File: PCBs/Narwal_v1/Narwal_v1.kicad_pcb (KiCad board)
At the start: 4 copper layers, 85 x 100 mm, 48 parts, among them IC1 SWITCH-HSWA4-63DR+, IC2 SWITCH-HSWA4-63DR+, J1 SMA-LPRS-CONNECTOR, J2 Conn_01x04, J3 Conn_01x04, SW1 SW_SPST, U1 HMC452ST89ETR, U2 PGA-103+, U3 RFM96W-433S2, U4 DS3231M

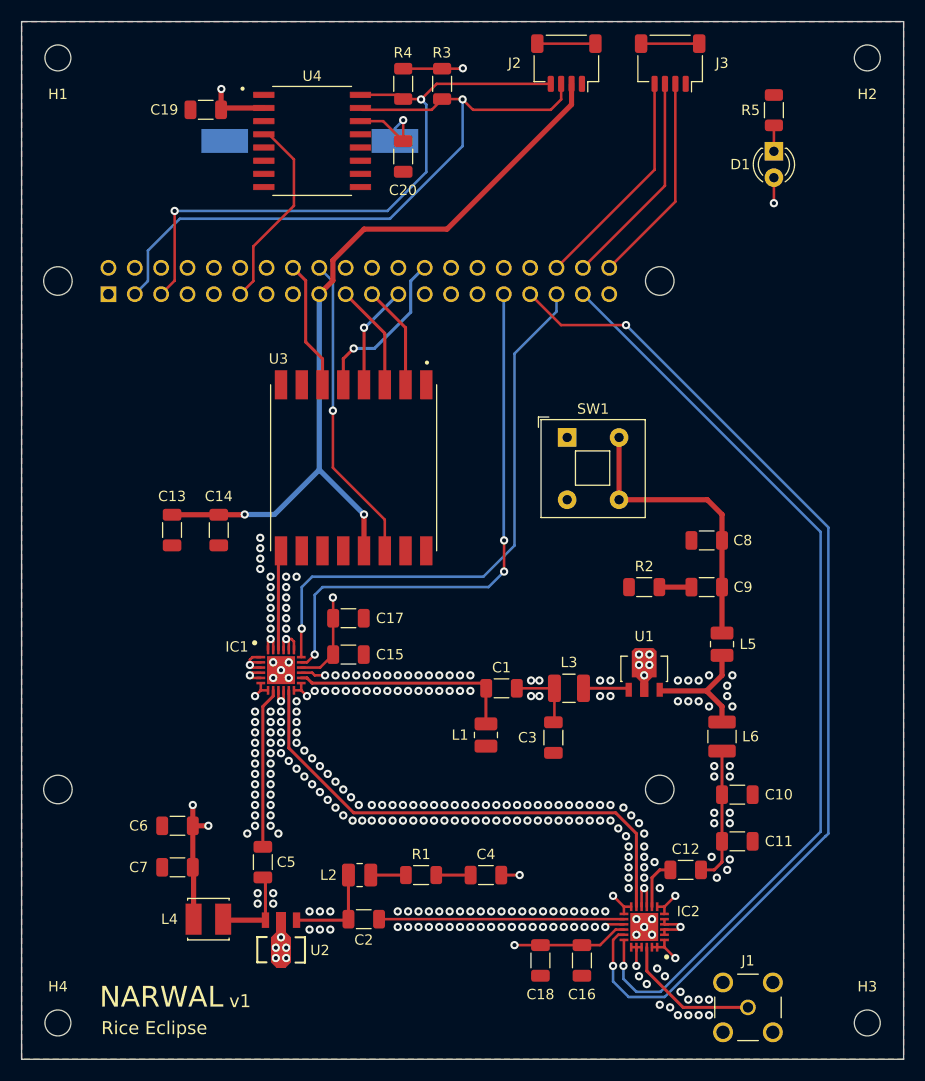
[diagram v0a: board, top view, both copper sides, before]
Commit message: power switch fixes, JLC compatibility changes
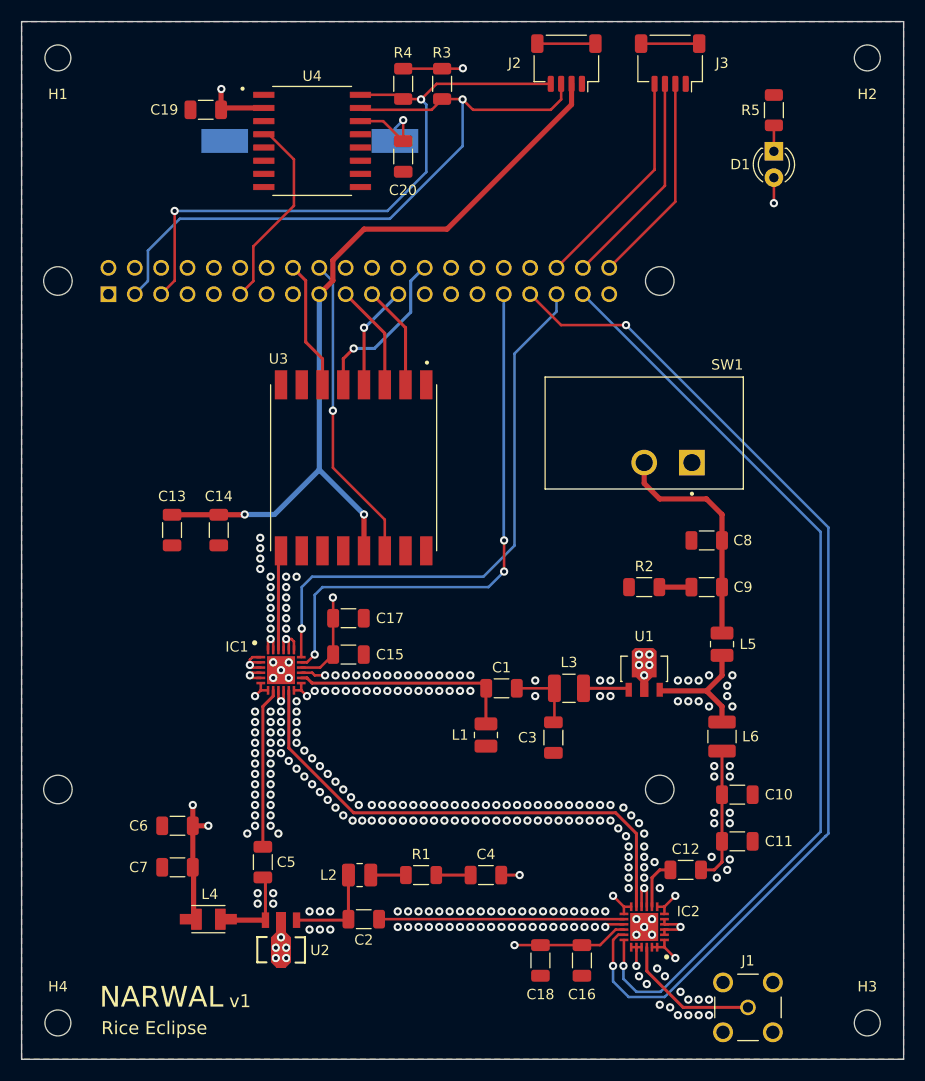
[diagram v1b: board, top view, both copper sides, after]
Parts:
- L4: value CHOKE-LQH44PN4R7MP0L -> CHOKE-LQH32NH4R7J23L; footprint Eclipse_RF_Footprints:CHOKE-LQH44PN4R7MP0L -> Eclipse_RF_Footprints:CHOKE-LQH32NH4R7J23L
- SW1: footprint Button_Switch_THT:SW_Push_2P1T_Toggle_CK_PVA1xxH1xxxxxxV2 -> Eclipse_RF_Footprints:SWITCH-L101011MS02Q
- moved SW1 7.43 mm to (160.0, 89.7), turned to 180 degrees
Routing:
- net Net-(C8-Pad1): track 27.9 -> 22.2 mm
- net GND: vias 299 -> 297
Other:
- rule pad_to_mask_clearance: 0 -> 0.05
- board text added: "JLCJLCJLCJLC"

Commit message: JLC-required silkscreen changes
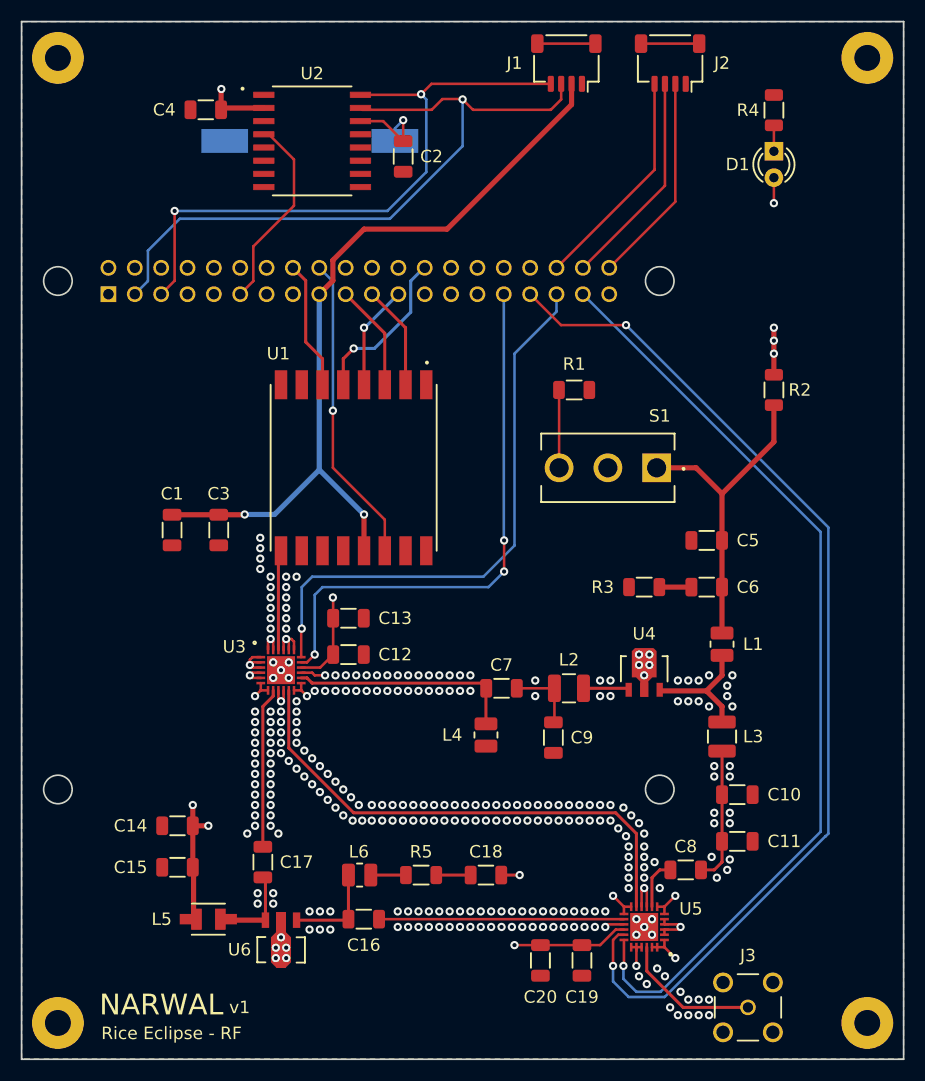
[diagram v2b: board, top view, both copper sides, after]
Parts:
- removed the R3 at (140.5, 56.0)
- removed the R4 at (136.8, 56.0)
- removed SW1: SW_SPST, Eclipse_RF_Footprints:SWITCH-L101011MS02Q
- added R1: 47K, Resistor_SMD:R_1206_3216Metric, F.Cu at (153.2, 85.5)
- added R2: 0R, Resistor_SMD:R_1206_3216Metric, F.Cu at (172.5, 85.5)
- added S1: 500SSP1S1M2QEA, Eclipse_RF_Footprints:SWITCH-500SSP1S1M2QEA, F.Cu at (156.5, 93.0)
- A1: value RPI-ZERO-ADA3708 -> RASPBERRY-PI
- BT1: value BATT-S8411-45R -> S8411-45R
- C12: renamed from C15; value 100n -> 100p
- C19: renamed from C16; value 100n -> 100p
- H1, H2, H3, H4: value MountingHole -> MountingHole_Pad; footprint MountingHole:MountingHole_2.5mm -> MountingHole:MountingHole_2.5mm_Pad
- J1: renamed from J2; value Conn_01x04 -> JST-SH
- J2: renamed from J3; value Conn_01x04 -> JST-SH
- J3: renamed from J1; value SMA-LPRS-CONNECTOR -> SMA-LPRS
- L5: renamed from L4; value CHOKE-LQH32NH4R7J23L -> LQH32NH4R7J23L
- R4: renamed from R5; value 154R -> 1K
- U1: renamed from U3; value RFM96W-433S2 -> RFM96W-433
- U3: renamed from IC1; value SWITCH-HSWA4-63DR+ -> HSWA4-63DR+
- U4: renamed from U1; value HMC452ST89ETR -> HMC452ST89
- U5: renamed from IC2; value SWITCH-HSWA4-63DR+ -> HSWA4-63DR+
- renumbered C13 to C1, C17 to C13, C6 to C14, C7 to C15, C2 to C16, C5 to C17, C4 to C18, C20 to C2, C18 to C20, C14 to C3, C19 to C4, C8 to C5, C9 to C6, C1 to C7, C12 to C8, C3 to C9, L5 to L1, L3 to L2, L6 to L3, L1 to L4, L2 to L6, R2 to R3, R1 to R5, U4 to U2, U2 to U6
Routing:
- net Net-(C5-Pad1): track 22.2 -> 31.4 mm
- net Net-(R1-Pad2): track 0.00 -> 7.49 mm
- net +5V: track 46.9 -> 45.7 mm, vias 7 -> 9
- net SCL: track 60.1 -> 60.8 mm
- net GND: vias 297 -> 296
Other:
- rule pad_to_mask_clearance: 0.05 -> 0
- board text added: "Rice Eclipse - RF"
- board text removed: "Rice Eclipse"

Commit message: final changes and fabrication
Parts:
- removed the R1 at (153.2, 85.5)
- D1: value LED -> PWR; footprint LED_THT:LED_D3.0mm -> LED_THT:LED_D5.0mm
- L2, L3: footprint Inductor_SMD:L_1210_3225Metric -> Inductor_SMD:L_0603_1608Metric_Pad1.05x0.95mm_HandSolder
- moved C9 0.75 mm to (152.0, 119.0)
- moved D1 0.73 mm to (172.5, 63.2)
- moved L5 0.50 mm to (117.5, 136.5)
- moved C7 0.25 mm to (146.2, 114.0)
- moved L2 0.25 mm to (153.0, 114.2)
- moved L3 0.10 mm to (167.5, 119.0)
- renumbered R2 to R1, R3 to R2, R4 to R3, R5 to R4
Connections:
- S1 pad 3: Net-(R1-Pad2) -> unconnected-(S1-Pad3)
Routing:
- net Net-(R1-Pad2): track 7.49 -> 0.00 mm
- net Net-(C17-Pad1): track 7.29 -> 8.62 mm
- net Net-(D1-Pad1): track 2.50 -> 3.23 mm
- net +5V: track 45.7 -> 46.4 mm
- net Net-(L1-Pad2): track 12.2 -> 12.8 mm
- net Net-(L2-Pad2): track 4.21 -> 4.74 mm
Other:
- board text added: "LNA"
- board text added: "NOAMP"
- board text added: "PA PWR"
- board text added: "PAMP"
- board text added: "RX"
- board text added: "TX"
- board text removed: "JLCJLCJLCJLC"
